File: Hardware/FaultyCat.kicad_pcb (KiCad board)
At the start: 2 copper layers, 51.2 x 124.2 mm, 136 parts, among them J1 Antenna, J10 TRIGGER_VREF, J2 BG306-02-A-2-0400-L-G, J3 Conn_01x10, J4 Header 2, J5 Header 4, J6 Input Power:2x AA Battery, J7 GLITCHER_EN, J8 ANALOG_PINS, J9 TRIGGER_IN, P1 USB_C_Plug_USB2.0, Q1 AO3422, Q2 AO3422, Q3 LDA111STR, Q4 RGT16BM65DTL, Q5 DMG3415U-7, Q7 IRLML2502, Q8 IRF7807PBF, SW1 TL3305AF260QG, SW2 ON, SW3 TL3305AF260QG, SW4 RESET, SW5 BOOT, SW6 TL3305AF260QG, SW7 SW_SP3T, T1 ATB322524, T2 ATB322524, U1 AP2112K-3.3, U2 W25Q16JV, U3 RP2040, U4 TXS0108EPW, U5 TLV75718PDBV, U6 SN74LVC1T45DBV, Y1 12Mhz

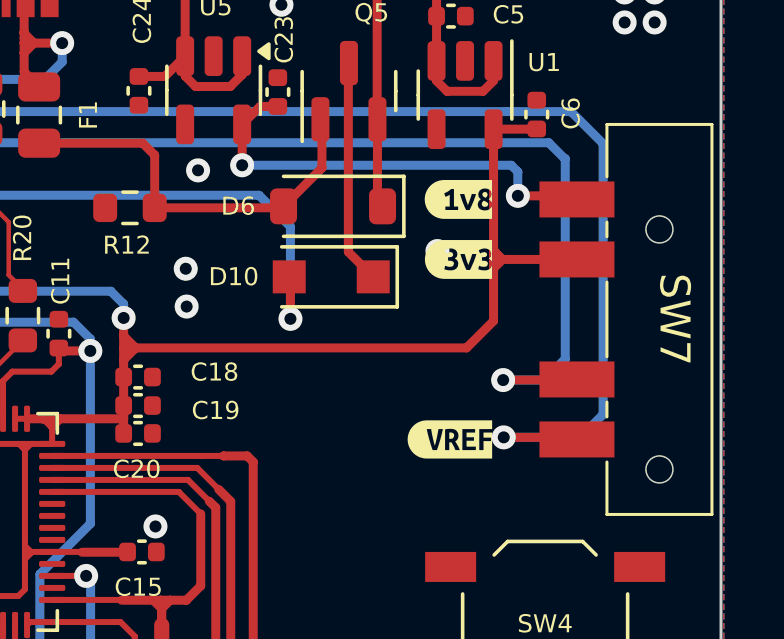
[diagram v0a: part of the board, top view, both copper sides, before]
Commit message: refactor(hw): change shape of labels on voltage selector
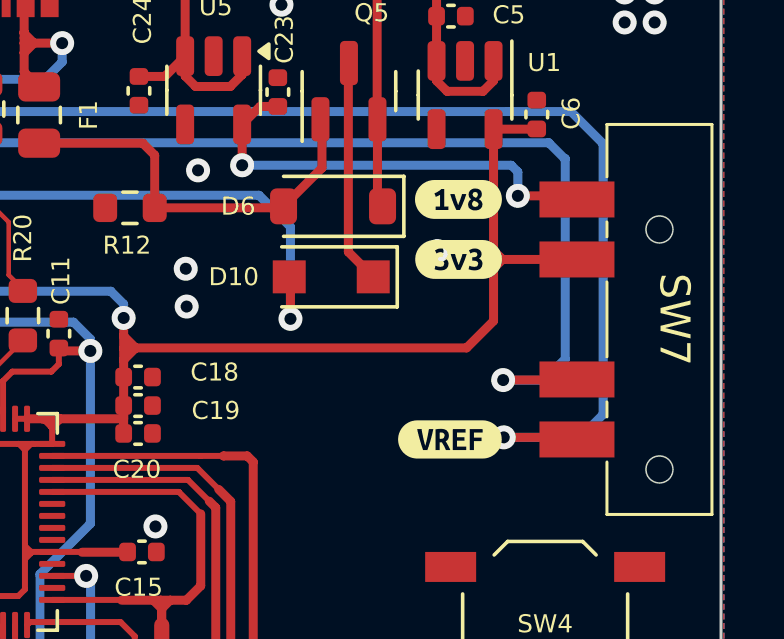
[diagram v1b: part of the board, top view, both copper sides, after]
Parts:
- removed kibuzzard-67AA359F: G***, kibuzzard-67AA359F
- removed kibuzzard-67AA35B7: G***, kibuzzard-67AA35B7
- removed kibuzzard-67AA35C3: G***, kibuzzard-67AA35C3
- added kibuzzard-681E4798: G***, kibuzzard-681E4798, F.Cu at (127.5, 39.9)
- added kibuzzard-681E47A0: G***, kibuzzard-681E47A0, F.Cu at (127.5, 41.9)
- added kibuzzard-681E47A5: G***, kibuzzard-681E47A5, F.Cu at (127.2, 47.9)

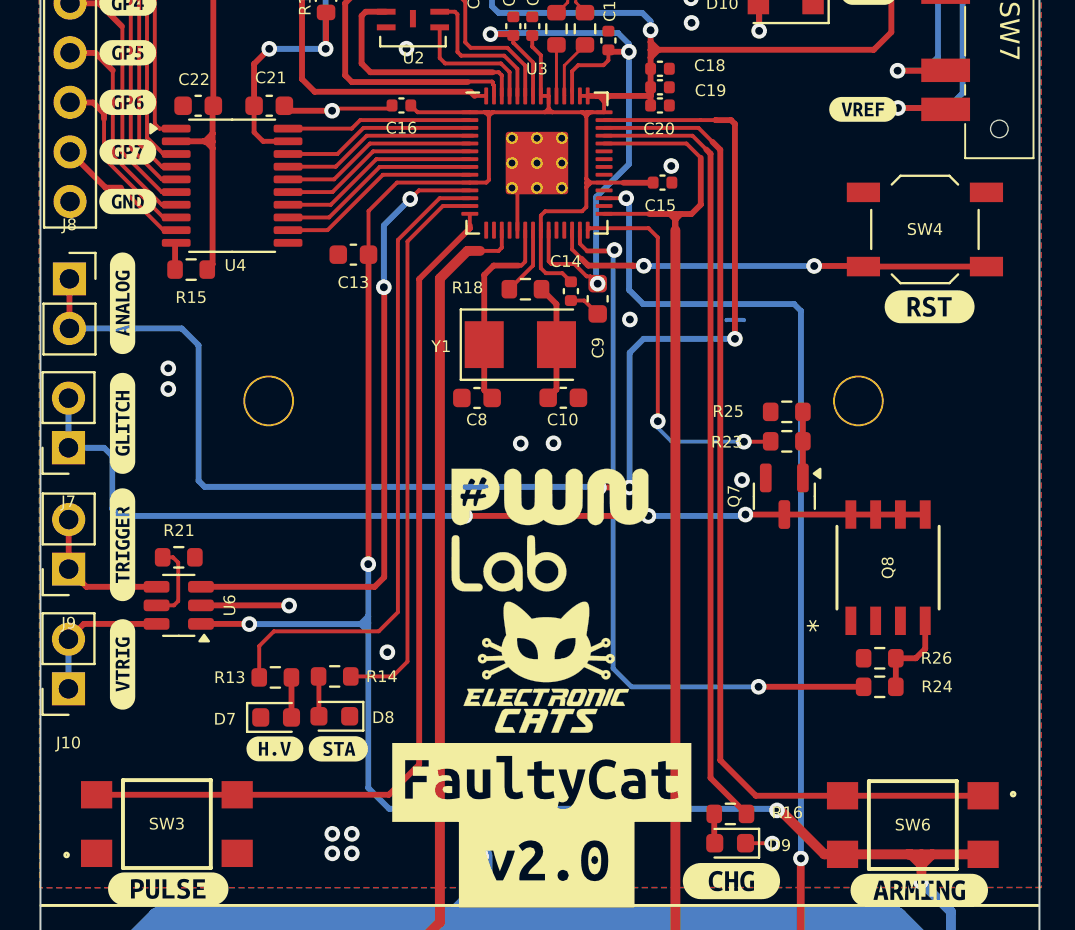
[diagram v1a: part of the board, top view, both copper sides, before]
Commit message: fix(hw): move components
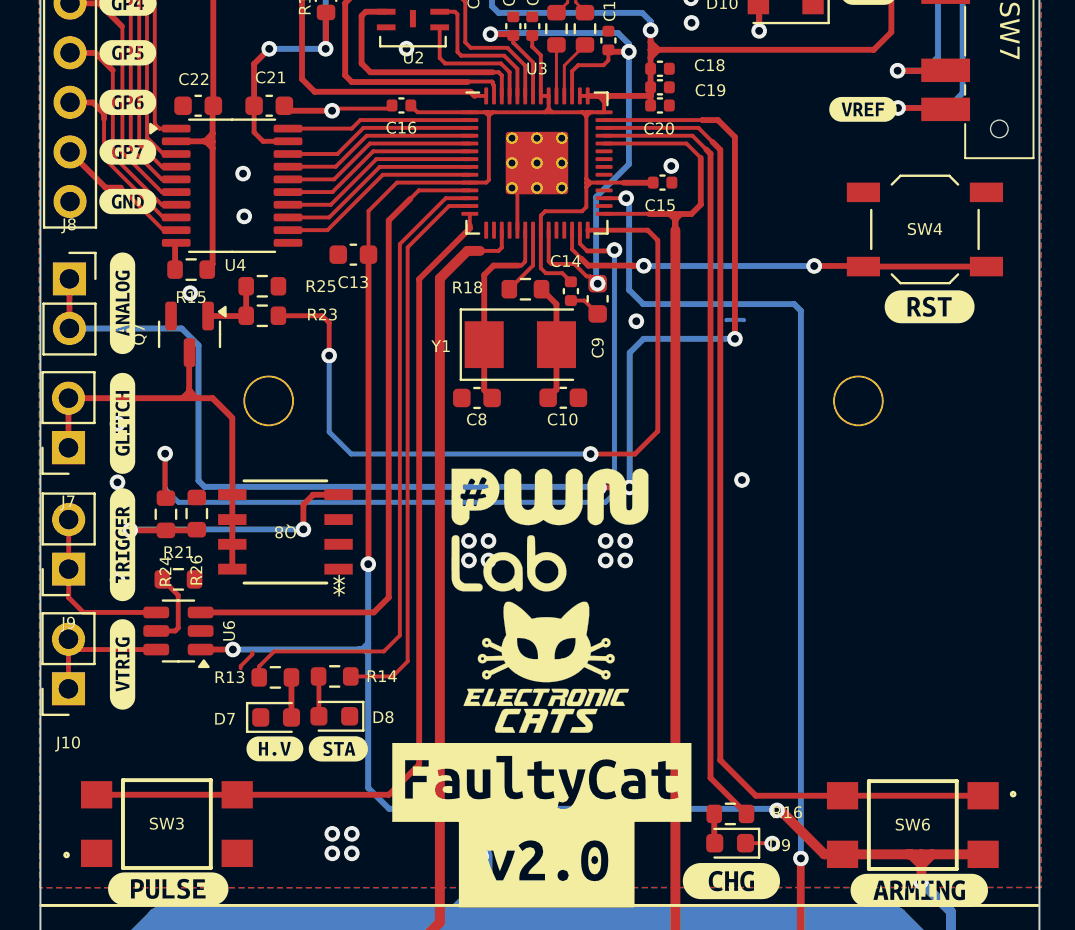
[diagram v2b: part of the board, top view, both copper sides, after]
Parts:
- moved R24 37.6 mm to (91.5, 68.6), turned to -90 degrees
- moved R26 35.8 mm to (93.1, 68.6), turned to -90 degrees
- moved Q7 31.6 mm to (92.7, 59.4)
- moved Q8 30.9 mm to (97.6, 69.5), turned to 180 degrees
- moved R23 27.6 mm to (96.4, 58.5), turned to 0 degrees
- moved R25 27.6 mm to (96.4, 57.0), turned to 0 degrees
- moved U6 1.31 mm to (92.1, 74.6)
- moved R21 1.13 mm to (92.1, 72.0)
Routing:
- net /GLITCHER: track 49.5 -> 23.9 mm, vias 3 -> 0
- net /LPGLITCH2: track 19.7 -> 39.7 mm
- net Net-(Q8-G): track 4.60 -> 15.6 mm, vias 0 -> 2
- net /HPGLITCH2: track 37.3 -> 42.8 mm
- net GND: track 171.2 -> 167.8 mm, vias 28 -> 36
- net /TRIGGER_IN: track 7.41 -> 8.80 mm
- net /TRIGGER: track 32.8 -> 34.0 mm, vias 2 -> 0

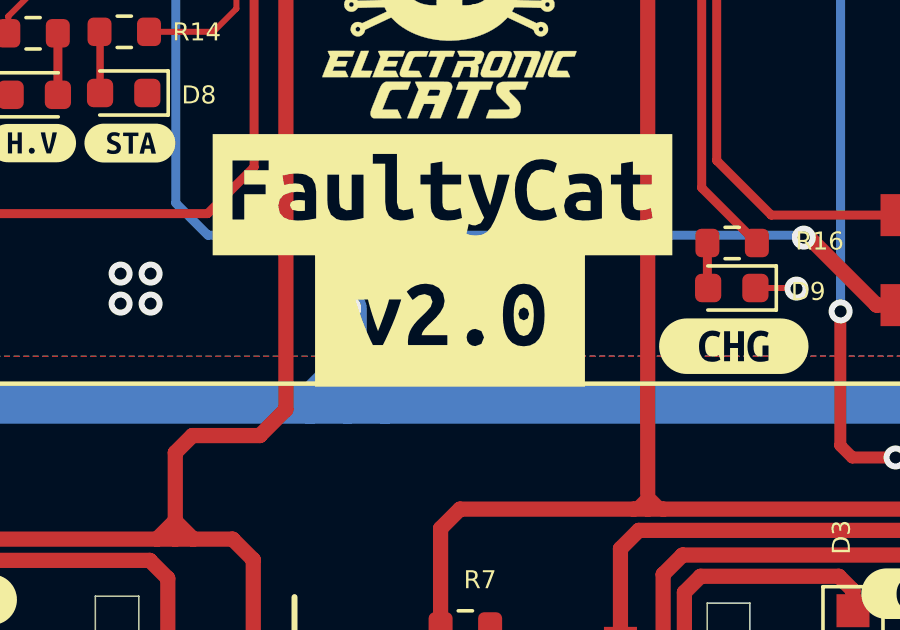
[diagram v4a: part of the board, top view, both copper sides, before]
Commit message: feat(Hw):Update_Labels
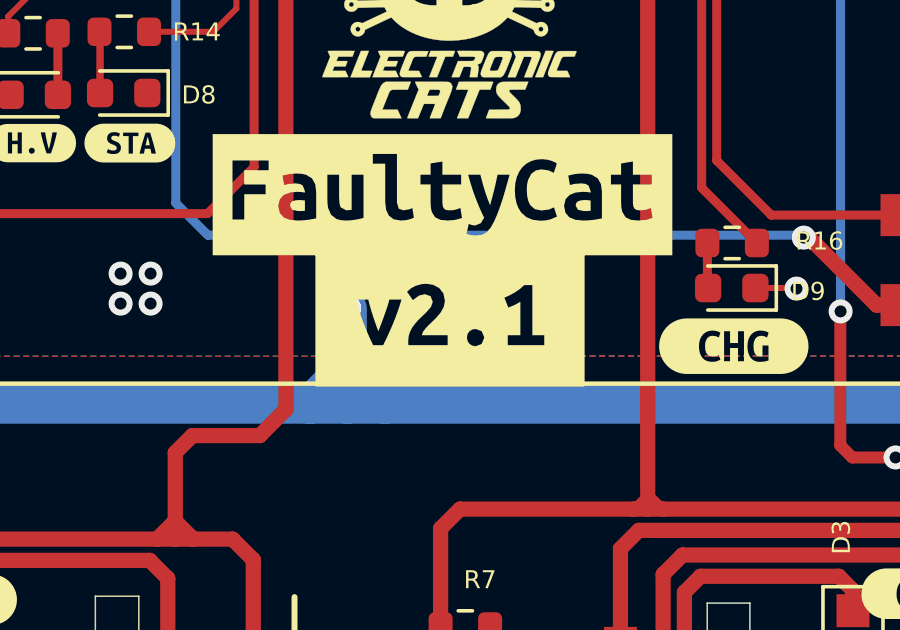
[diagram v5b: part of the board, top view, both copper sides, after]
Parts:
- removed kibuzzard-67AA305E: G***, kibuzzard-67AA305E
- added kibuzzard-68509CA3: G***, kibuzzard-68509CA3, F.Cu at (111.0, 86.4)

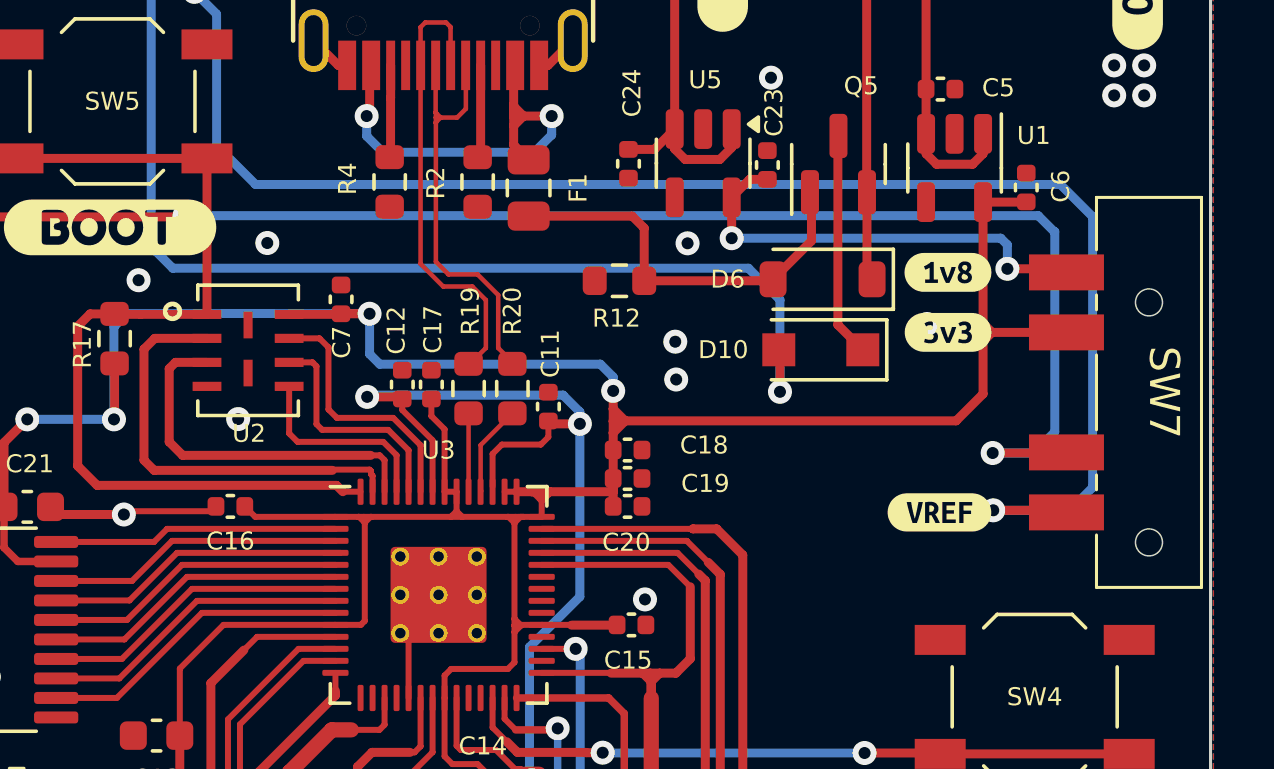
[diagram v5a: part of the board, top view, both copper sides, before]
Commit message: fix(hw): change switch orientation
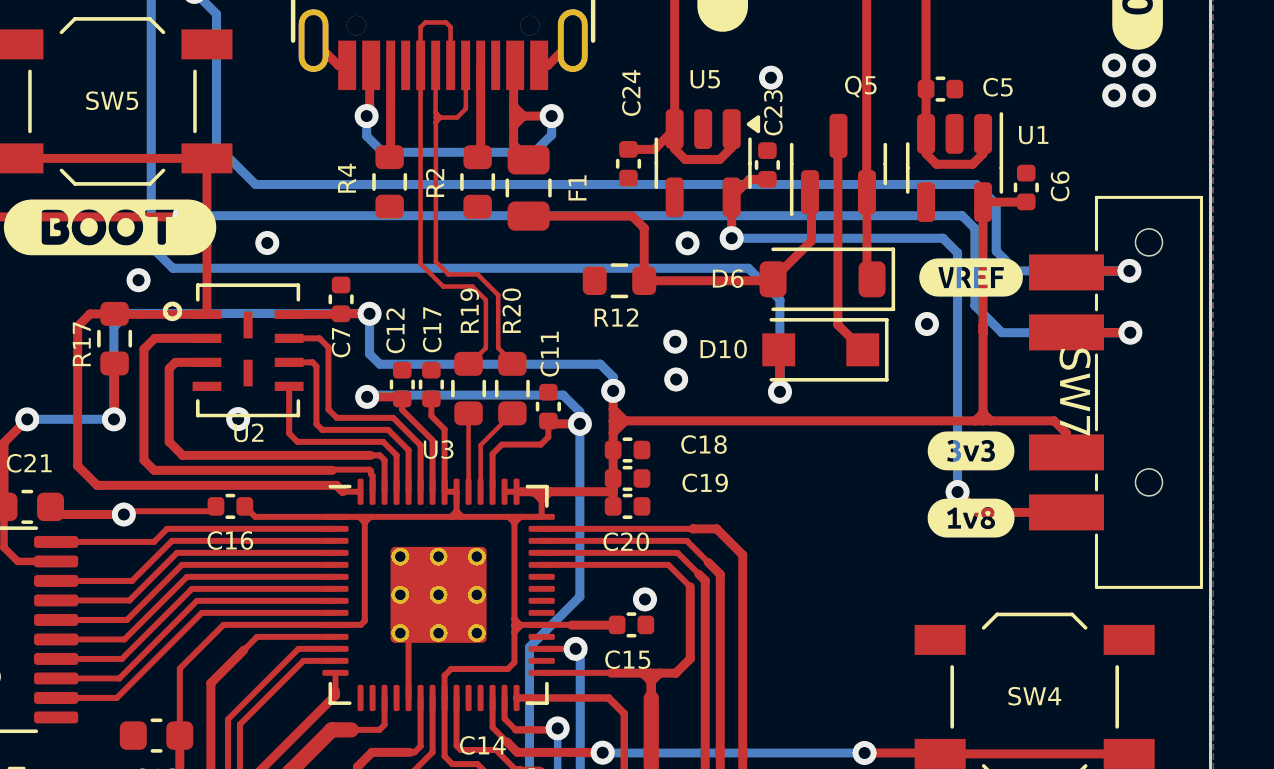
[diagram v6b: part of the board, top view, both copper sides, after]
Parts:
- moved kibuzzard-681E4798 8.23 mm to (128.2, 48.1)
- moved kibuzzard-681E47A5 7.90 mm to (128.2, 40.1)
- moved kibuzzard-681E47A0 4.02 mm to (128.2, 45.9)
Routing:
- net /VREF: track 66.8 -> 56.9 mm
- net +1V8: track 14.9 -> 22.4 mm
- net /VREFOUT: track 69.0 -> 65.1 mm
- net +3V3: track 233.4 -> 234.9 mm
